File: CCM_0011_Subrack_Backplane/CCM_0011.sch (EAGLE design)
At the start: 23 parts, among them J1 PIN2F061.100, J2 PIN2F061.220, X1 FAB64S, X10 FAB64S, X11 FAB64S, X12 FAB64S, X13 FAB64S, X14 FAB64S, X15 FAB64S, X16 FAB64S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

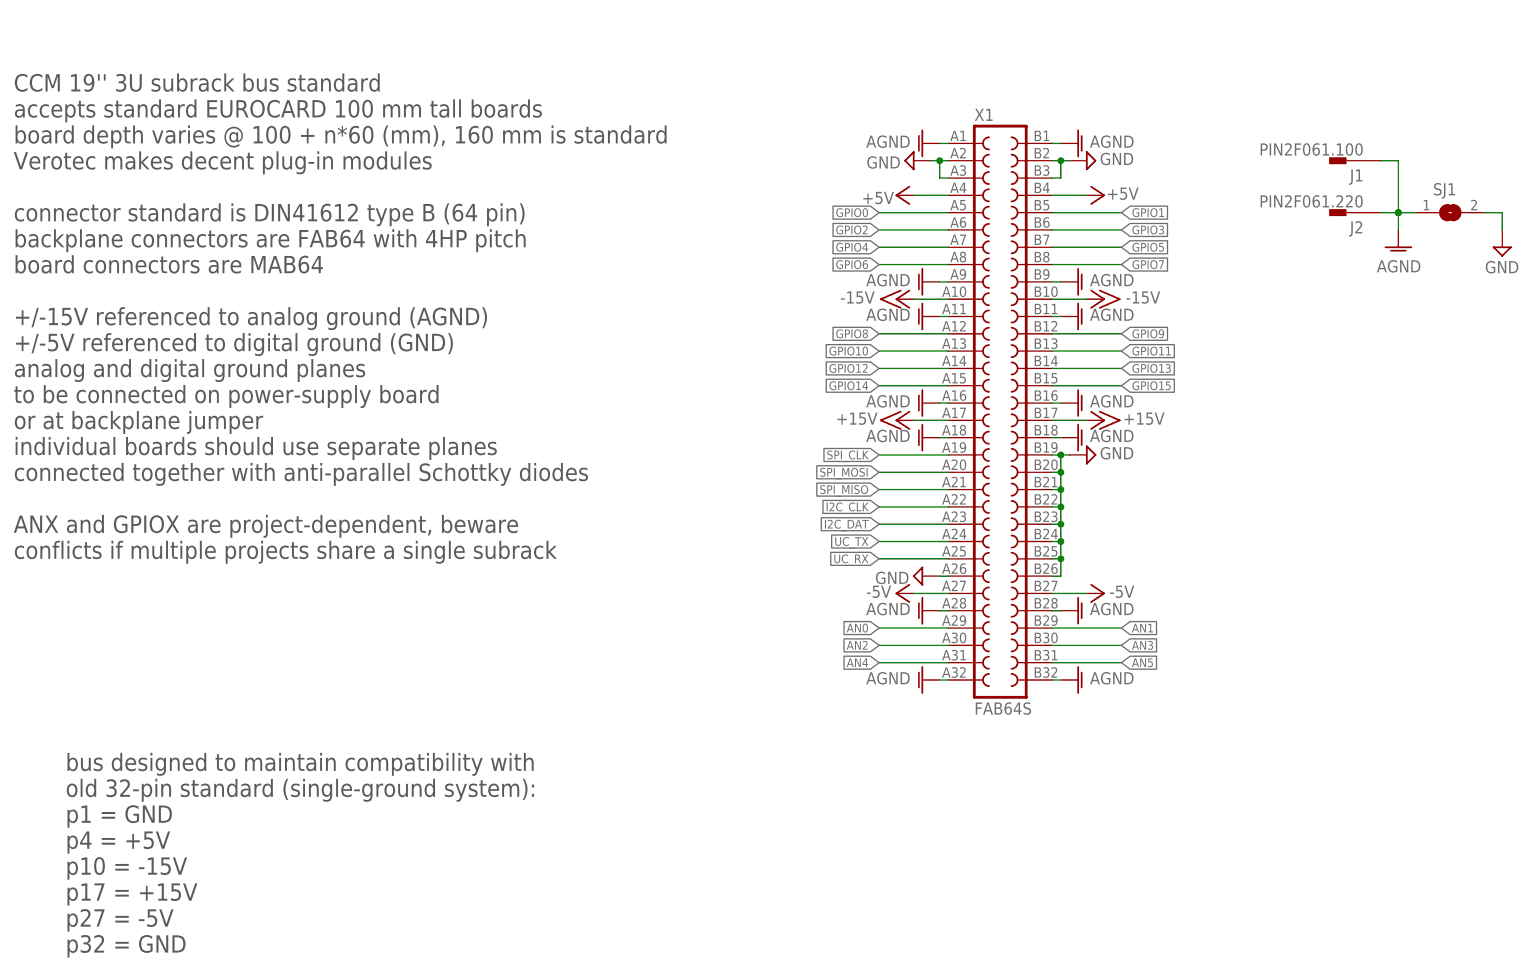
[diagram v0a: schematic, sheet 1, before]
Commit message: Shutter driver added.
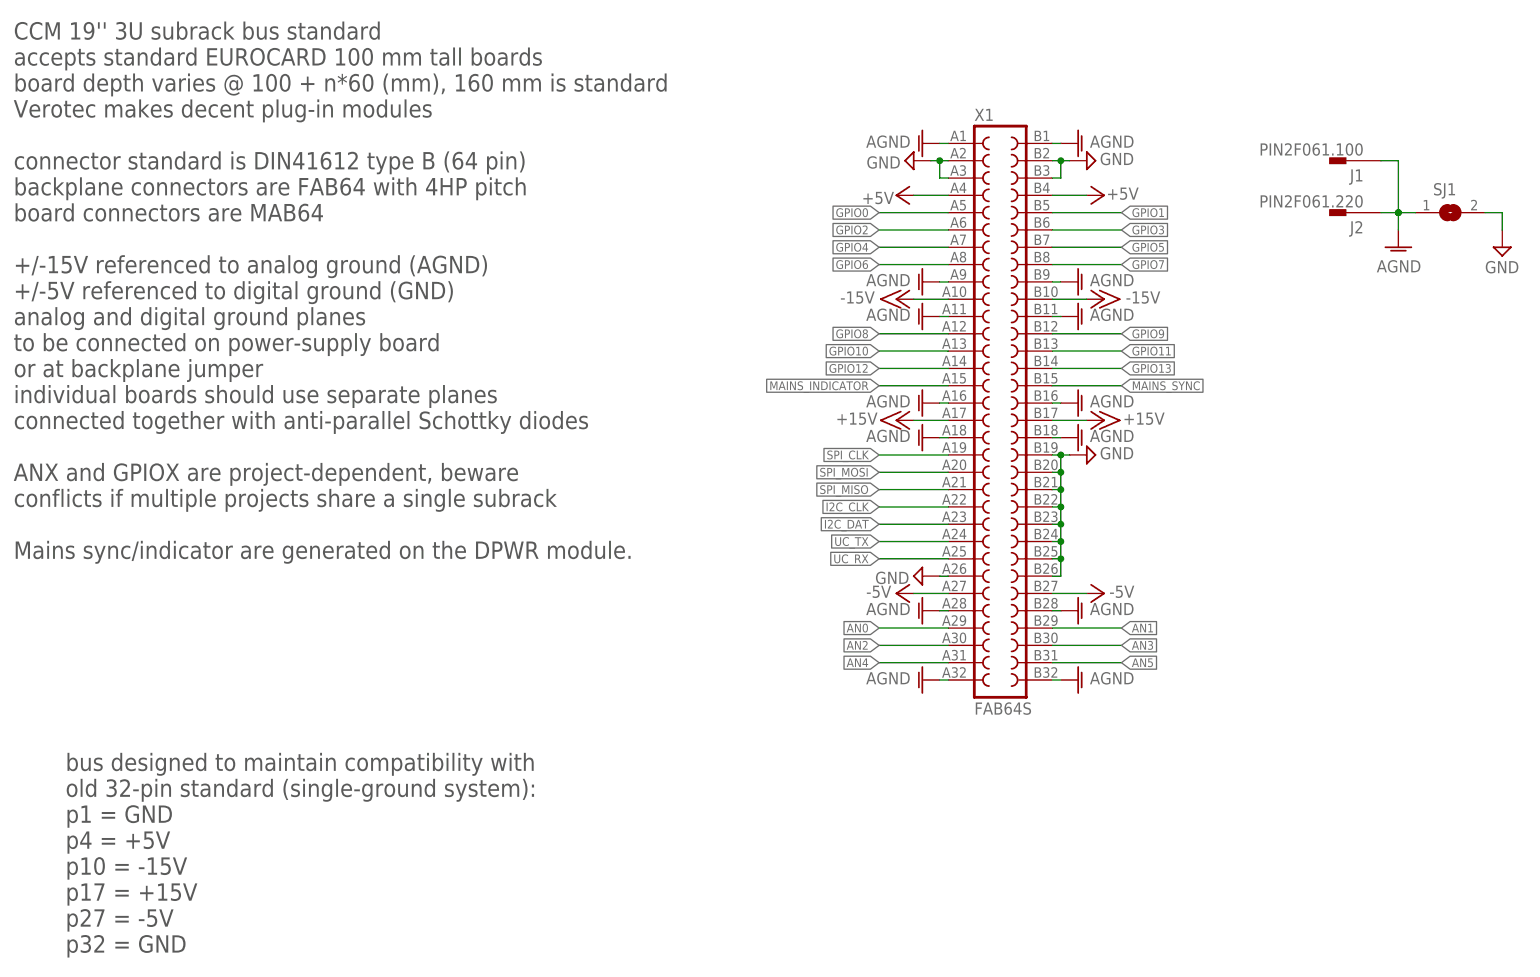
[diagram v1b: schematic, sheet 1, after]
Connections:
- new net MAINS_INDICATOR: X1.A15
- new net MAINS_SYNC: X1.B15
- net GPIO14: no longer X1.A15
- net GPIO15: no longer X1.B15
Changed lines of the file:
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@@
 <?xml version="1.0" encoding="utf-8"?>
 <!DOCTYPE eagle SYSTEM "eagle.dtd">
-<eagle version="8.6.0">
+<eagle version="9.0.1">
 <drawing>
 <settings>
@@
 <setting verticaltext="up"/>
 </settings>
-<grid distance="0.025" unitdist="inch" unit="inch" style="lines" multiple="4" display="yes" altdistance="0.01" altunitdist="inch" altunit="inch"/>
+<grid distance="0.1" unitdist="inch" unit="inch" style="lines" multiple="1" display="no" altdistance="0.01" altunitdist="inch" altunit="inch"/>
 <layers>
 <layer number="1" name="Top" color="4" fill="1" visible="no" active="no"/>
@@
 connected together with anti-parallel Schottky diodes
 ANX and GPIOX are project-dependent, beware
-conflicts if multiple projects share a single subrack</text>
+conflicts if multiple projects share a single subrack
+Mains sync/indicator are generated on the DPWR module.</text>
 </plain>
 <instances>
@@
 <label x="139.7" y="99.06" size="1.27" layer="95" rot="R180" xref="yes"/>
 <pinref part="X1" gate="G$1" pin="A14"/>
-</segment>
-</net>
-<net name="GPIO14" class="0">
-<segment>
-<wire x1="149.86" y1="96.52" x2="139.7" y2="96.52" width="0.1524" layer="91"/>
-<label x="139.7" y="96.52" size="1.27" layer="95" rot="R180" xref="yes"/>
-<pinref part="X1" gate="G$1" pin="A15"/>
 </segment>
 </net>
@@
 <label x="175.26" y="99.06" size="1.27" layer="95" rot="MR180" xref="yes"/>
 <pinref part="X1" gate="G$1" pin="B14"/>
-</segment>
-</net>
-<net name="GPIO15" class="0">
-<segment>
-<wire x1="165.1" y1="96.52" x2="175.26" y2="96.52" width="0.1524" layer="91"/>
-<label x="175.26" y="96.52" size="1.27" layer="95" rot="MR180" xref="yes"/>
-<pinref part="X1" gate="G$1" pin="B15"/>
 </segment>
 </net>
@@
 </segment>
 </net>
+<net name="MAINS_SYNC" class="0">
+<segment>
+<wire x1="165.1" y1="96.52" x2="175.26" y2="96.52" width="0.1524" layer="91"/>
+<label x="175.26" y="96.52" size="1.27" layer="95" rot="MR180" xref="yes"/>
+<pinref part="X1" gate="G$1" pin="B15"/>
+</segment>
+</net>
+<net name="MAINS_INDICATOR" class="0">
+<segment>
+<wire x1="149.86" y1="96.52" x2="139.7" y2="96.52" width="0.1524" layer="91"/>
+<label x="139.7" y="96.52" size="1.27" layer="95" rot="R180" xref="yes"/>
+<pinref part="X1" gate="G$1" pin="A15"/>
+</segment>
+</net>
